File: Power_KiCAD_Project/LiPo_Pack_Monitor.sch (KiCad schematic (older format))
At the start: 36 parts, among them Q1 CSD17501Q5A, Q2 BSS84PH6327XTSA2, Q3 CSD17501Q5A, SW1 Reboot, U3 BQ76920PW

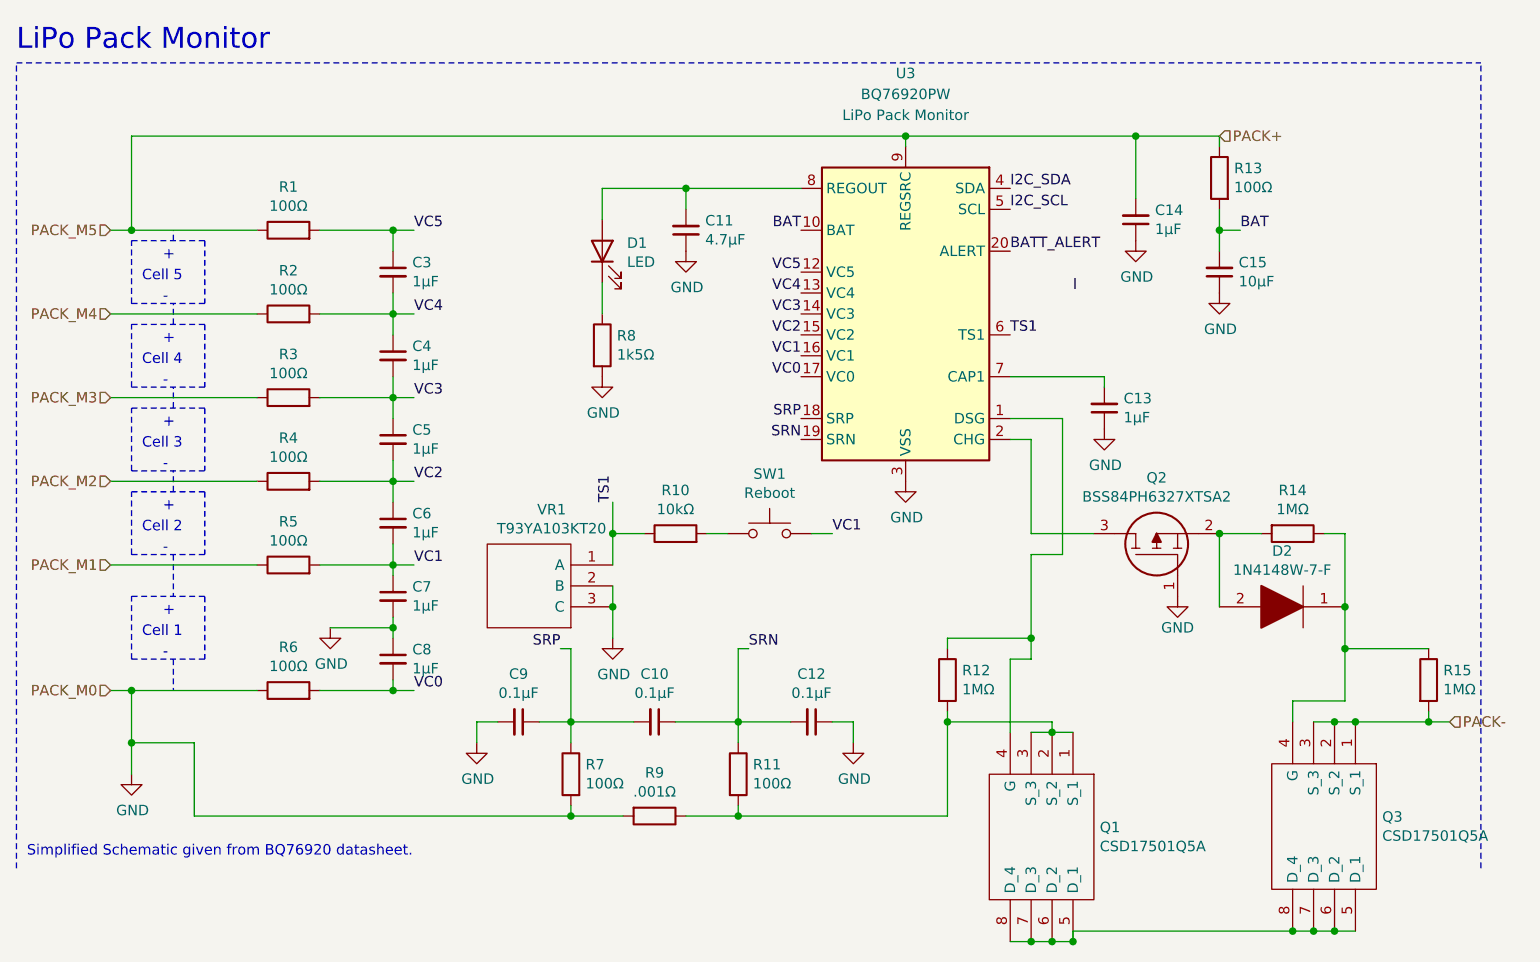
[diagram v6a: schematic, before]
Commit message: Changes to PCB
re did the pcb and added a "switch"
basically its just an xt60 connector in series with the other ones that needs to be shorted for the board to get power
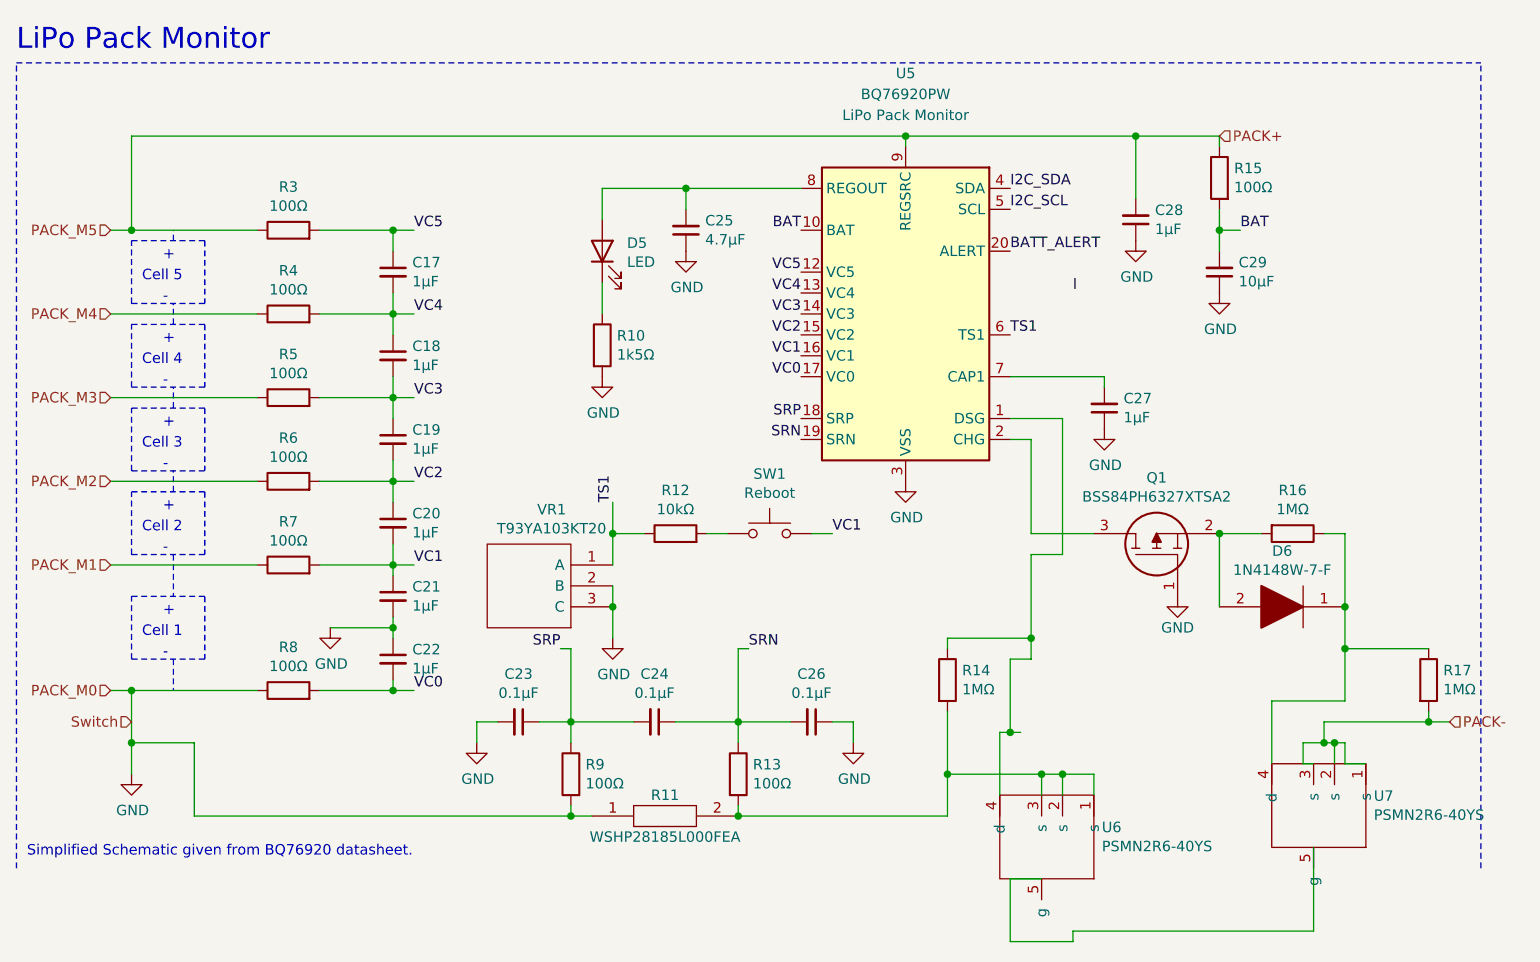
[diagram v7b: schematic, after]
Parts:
- removed Q1, Q3: CSD17501Q5A, SamacSys_Parts:Q5A, symbol SamacSys_Parts:CSD17501Q5A
- removed R9: .001Ω, Resistor_SMD:R_0603_1608Metric, symbol Device:R
- added R11: WSHP28185L000FEA, RESC7146X175N, symbol SamacSys_Parts:WSHP28185L000FEA
- added U6, U7: PSMN2R6-40YS, TO127P600X120-5N:TO127P600X120-5N, symbol 1-747301-6:PSMN2R6-40YS
- renumbered C3 to C17, C4 to C18, C5 to C19, C6 to C20, C7 to C21, C8 to C22, C9 to C23, C10 to C24, C11 to C25, C12 to C26, C13 to C27, C14 to C28, C15 to C29, D1 to D5, D2 to D6, Q2 to Q1, R8 to R10, R10 to R12, R11 to R13, R12 to R14, R13 to R15, R14 to R16, R15 to R17, R1 to R3, R2 to R4, R3 to R5, R4 to R6, R5 to R7, R6 to R8, R7 to R9, U3 to U5
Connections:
- net GND: now also R11.1
- net PACK-: now also U7.1 (s), U7.2 (s), U7.3 (s)
- net at R14.1, U5.1 (DSG): now also U6.4 (d)
- net at R13.2, R14.2: now also R11.2, U6.1 (s), U6.2 (s), U6.3 (s)
- net at D6.1, R16.1, R17.1: now also U7.4 (d)
- new net: U6.5 (g), U7.5 (g)
